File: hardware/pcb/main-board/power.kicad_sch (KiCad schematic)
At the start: 16 parts, among them SW501 NO POP, SW502 NO POP, U501 PT4110

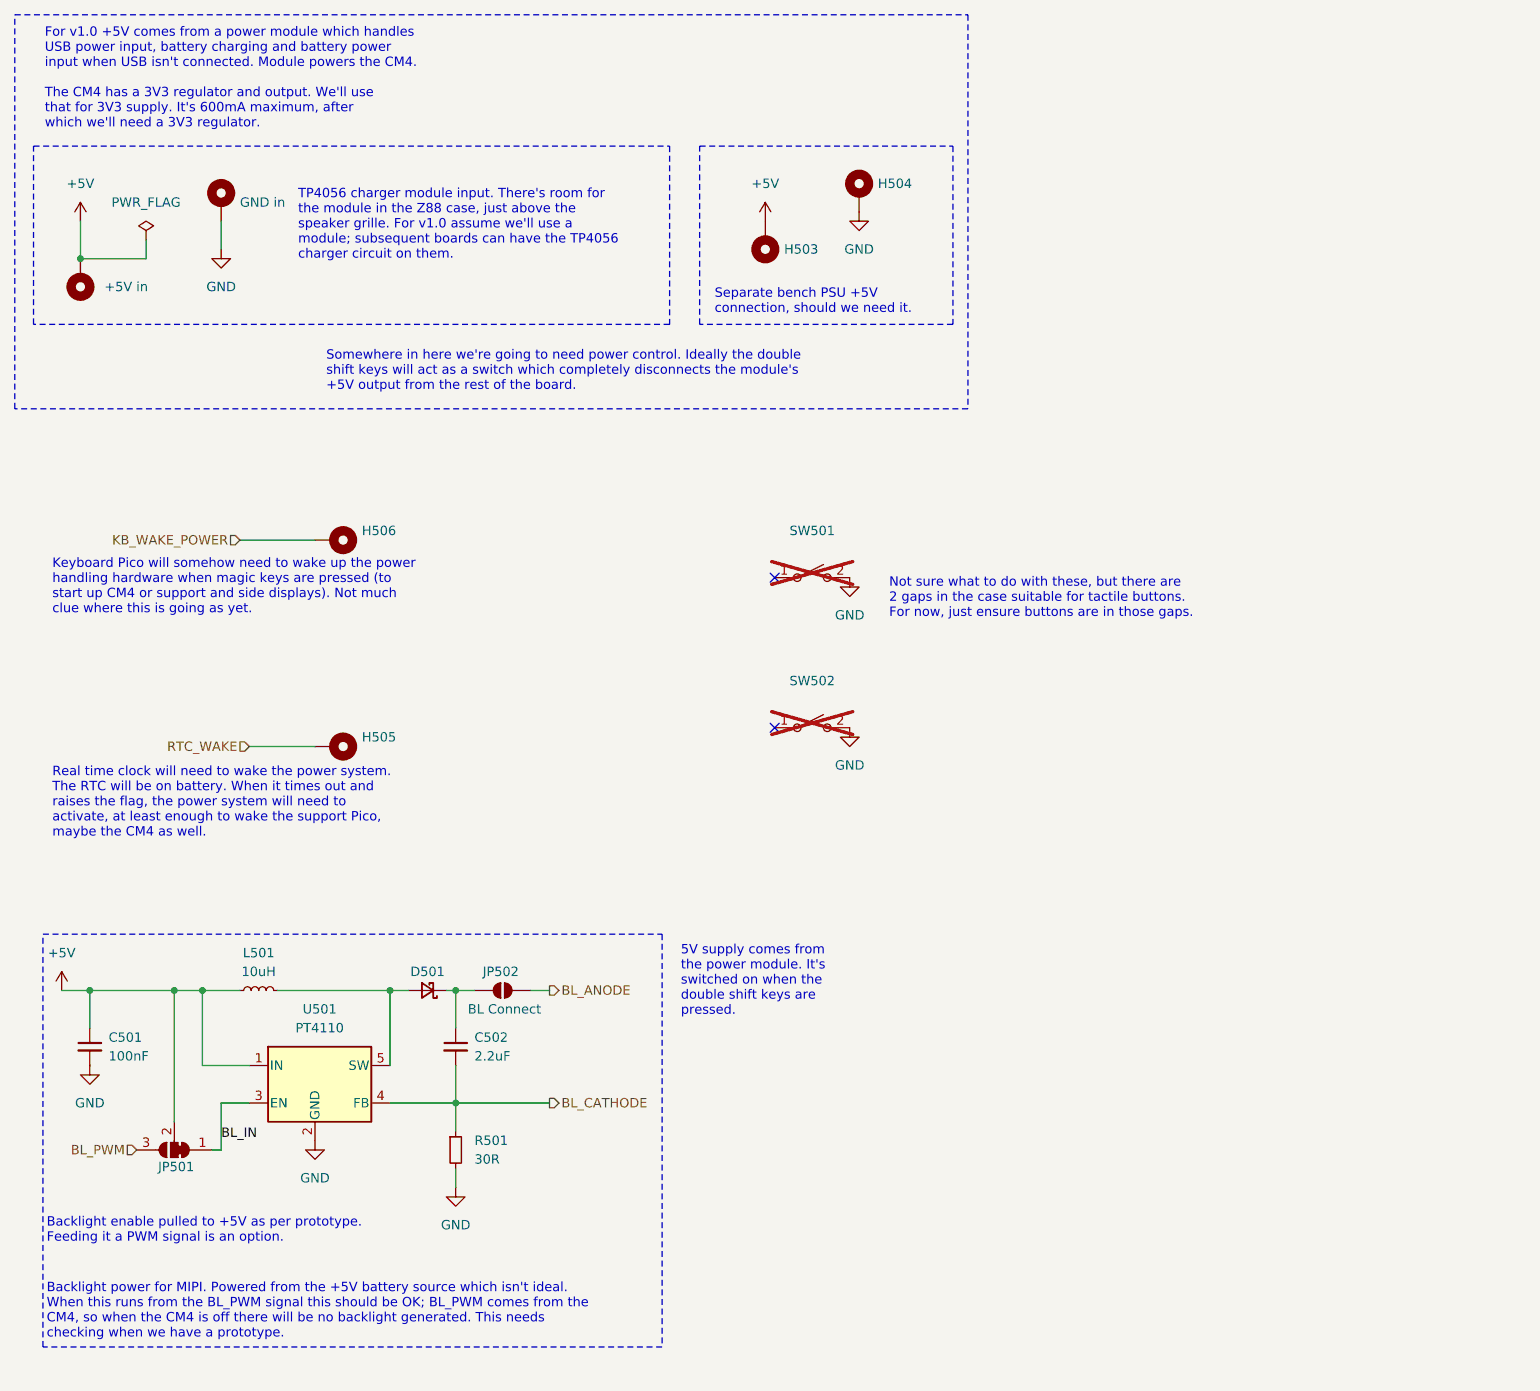
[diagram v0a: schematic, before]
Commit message: start next board iteration, add latch and pico power bits
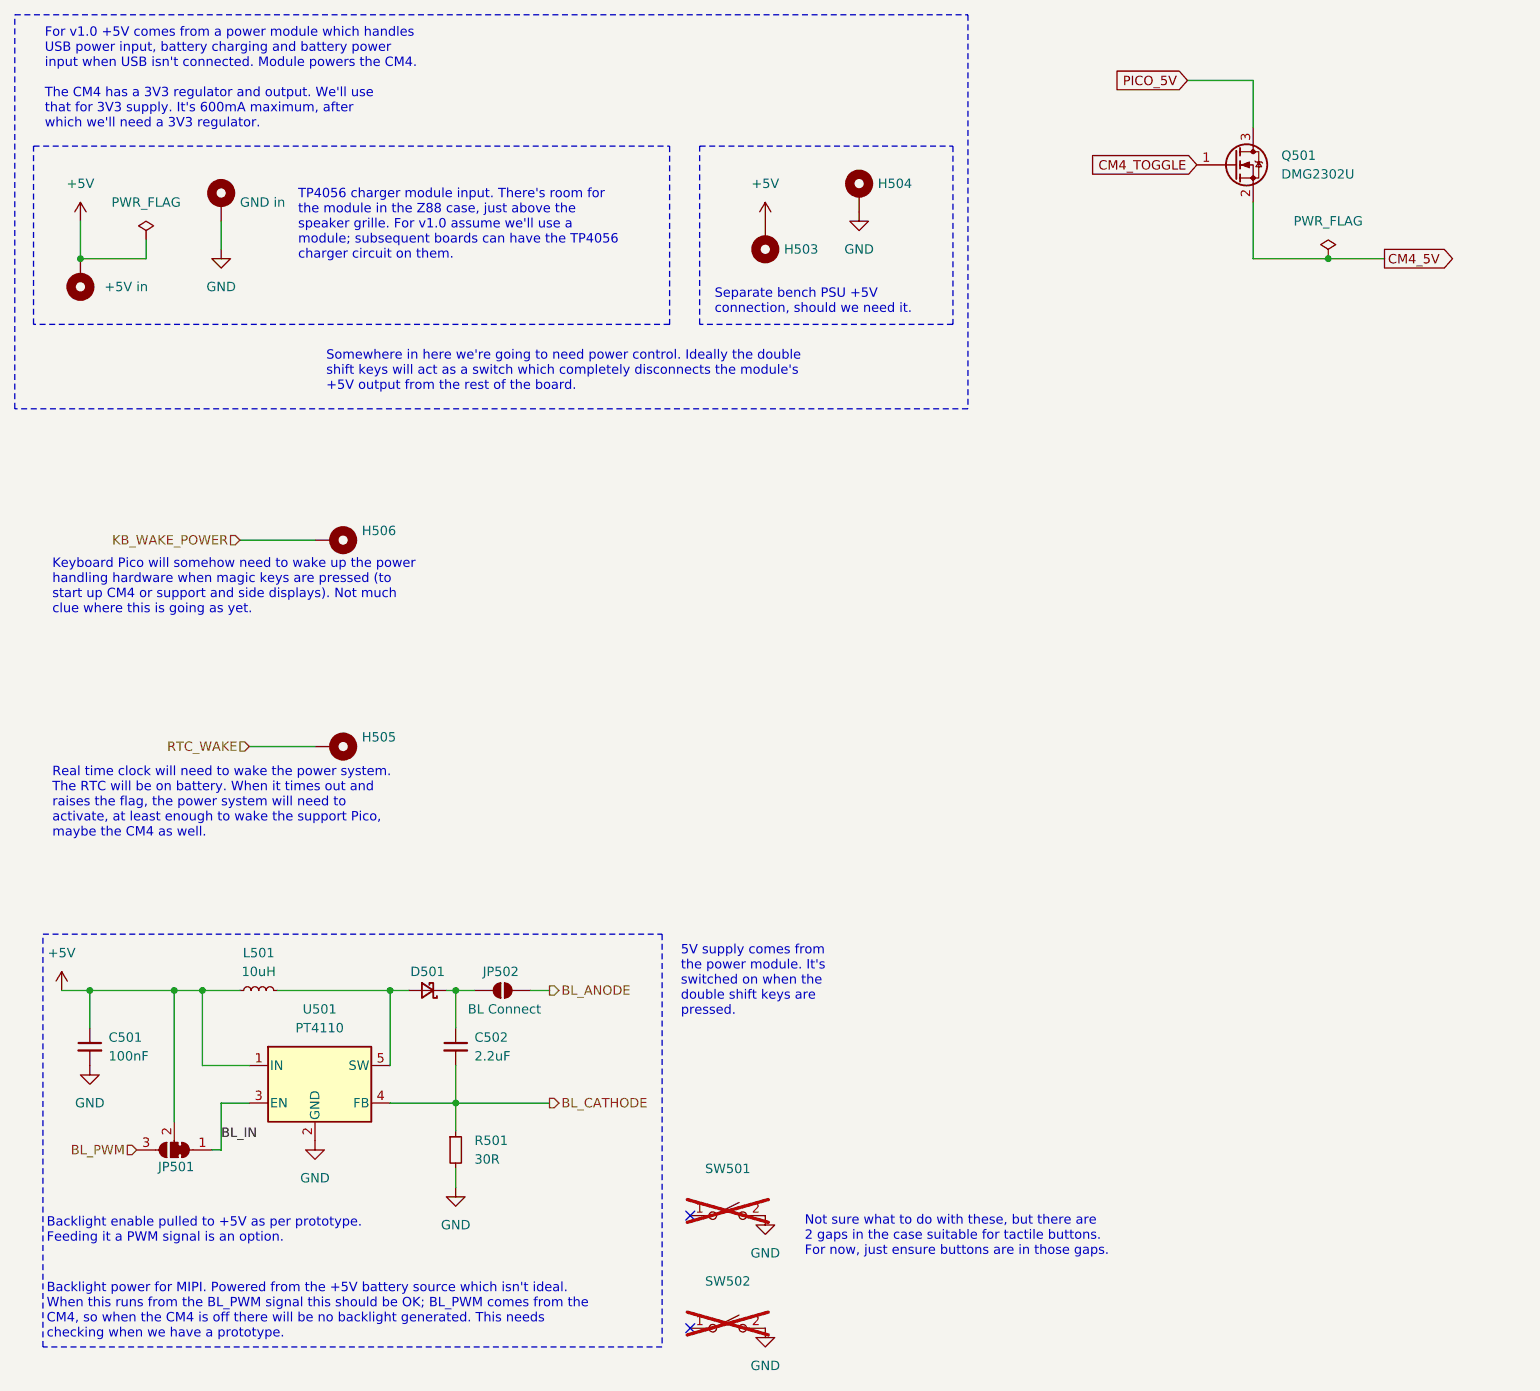
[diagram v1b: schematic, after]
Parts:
- added Q501: DMG2302U, Package_TO_SOT_SMD:SOT-23, symbol Transistor_FET:DMG2302U
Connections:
- new net CM4_5V: Q501.2 (S)
- new net CM4_TOGGLE: Q501.1 (G)
- new net PICO_5V: Q501.3 (D)
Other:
- moved on the sheet: SW501, SW502

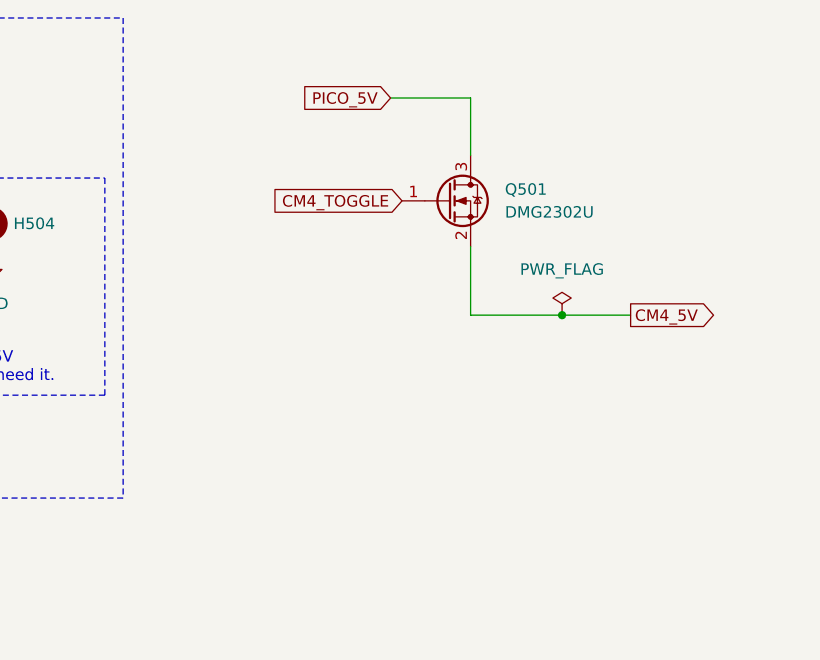
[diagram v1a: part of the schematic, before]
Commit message: CM4 power switch
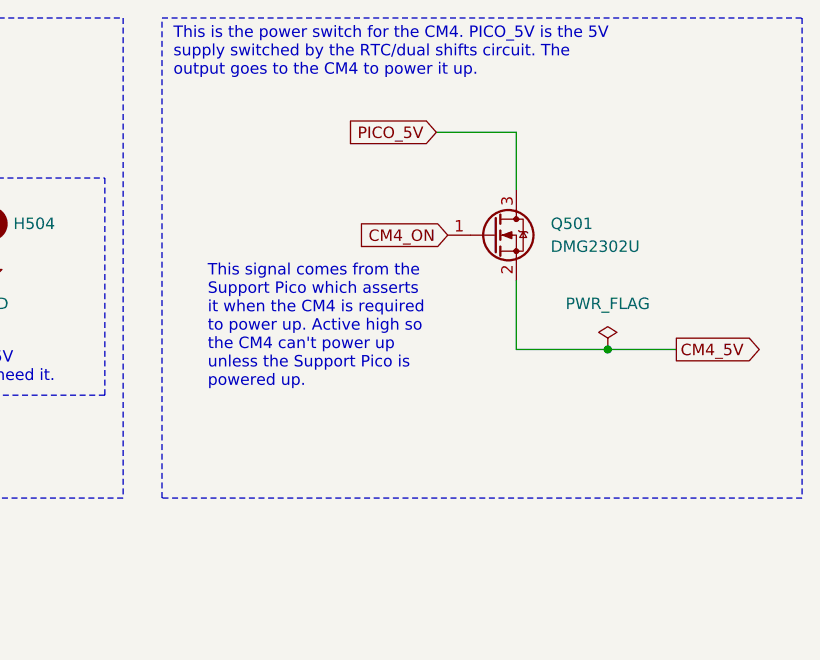
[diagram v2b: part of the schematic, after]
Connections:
- net CM4_TOGGLE renamed CM4_ON
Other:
- note added: "This is the power switch for the CM4. PICO_5V is the 5V supply switched by the RTC/dual shifts circuit. The output goes to the CM4 to power it up."
- note added: "This signal comes from the Support Pico which asserts it when the CM4 is required to power up. Active high so the CM4 can't power up unless the Support Pico is powered up."
- moved on the sheet: Q501
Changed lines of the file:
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@@
 	)
 	(junction
-		(at 190.5 46.99)
+		(at 195.58 50.8)
 		(diameter 0)
 		(color 0 0 0 0)
@@
 	(wire
 		(pts
-			(xy 180.34 22.86) (xy 180.34 29.21)
+			(xy 185.42 26.67) (xy 185.42 33.02)
 		)
 		(stroke
@@
 	(wire
 		(pts
-			(xy 180.34 39.37) (xy 180.34 46.99)
+			(xy 185.42 43.18) (xy 185.42 50.8)
 		)
 		(stroke
@@
 	(wire
 		(pts
-			(xy 171.45 22.86) (xy 180.34 22.86)
-		)
-		(stroke
-			(width 0)
-			(type default)
-		)
-	)
-	(wire
-		(pts
-			(xy 180.34 46.99) (xy 190.5 46.99)
+			(xy 176.53 26.67) (xy 185.42 26.67)
+		)
+		(stroke
+			(width 0)
+			(type default)
+		)
+	)
+	(wire
+		(pts
+			(xy 185.42 50.8) (xy 195.58 50.8)
 		)
 		(stroke
@@
 	(wire
 		(pts
-			(xy 190.5 46.99) (xy 198.12 46.99)
+			(xy 195.58 50.8) (xy 203.2 50.8)
 		)
 		(stroke
@@
 		(start 105.41 31.75)
 		(end 139.7 55.88)
+		(stroke
+			(width 0)
+			(type dash)
+		)
+		(fill
+			(type none)
+		)
+	)
+	(rectangle
+		(start 146.05 13.97)
+		(end 217.17 67.31)
 		(stroke
 			(width 0)
@@
 		)
 	)
+	(text "This signal comes from the\nSupport Pico which asserts\nit when the CM4 is required\nto power up. Active high so\nthe CM4 can't power up\nunless the Support Pico is\npowered up."
+		(exclude_from_sim no)
+		(at 151.13 48.26 0)
+		(effects
+			(font
+				(size 1.27 1.27)
+			)
+			(justify left)
+		)
+	)
 	(text "TP4056 charger module input. There's room for\nthe module in the Z88 case, just above the\nspeaker grille. For v1.0 assume we'll use a\nmodule; subsequent boards can have the TP4056\ncharger circuit on them."
 		(exclude_from_sim no)
@@
 		(exclude_from_sim no)
 		(at 17.78 91.44 0)
+		(effects
+			(font
+				(size 1.27 1.27)
+			)
+			(justify left)
+		)
+	)
+	(text "This is the power switch for the CM4. PICO_5V is the 5V\nsupply switched by the RTC/dual shifts circuit. The\noutput goes to the CM4 to power it up."
+		(exclude_from_sim no)
+		(at 147.32 17.78 0)
 		(effects
 			(font
@@
 		)
 	)
-	(global_label "CM4_TOGGLE"
+	(global_label "CM4_ON"
 		(shape input)
-		(at 172.72 34.29 180)
+		(at 177.8 38.1 180)
 		(fields_autoplaced yes)
 		(effects
@@
 		)
 		(property "Intersheetrefs" "${INTERSHEET_REFS}"
-			(at 158.4753 34.29 0)
+			(at 167.9095 38.1 0)
 			(effects
 				(font
@@
 	(global_label "PICO_5V"
 		(shape input)
-		(at 171.45 22.86 180)
+		(at 176.53 26.67 180)
 		(fields_autoplaced yes)
 		(effects
@@
 		)
 		(property "Intersheetrefs" "${INTERSHEET_REFS}"
-			(at 161.378 22.86 0)
+			(at 166.458 26.67 0)
 			(effects
 				(font
@@
 	(global_label "CM4_5V"
 		(shape output)
-		(at 198.12 46.99 0)
+		(at 203.2 50.8 0)
 		(fields_autoplaced yes)
 		(effects
@@
 		)
 		(property "Intersheetrefs" "${INTERSHEET_REFS}"
-			(at 207.6476 46.99 0)
+			(at 212.7276 50.8 0)
 			(effects
 				(font
@@
 	(symbol
 		(lib_id "Transistor_FET:DMG2302U")
-		(at 177.8 34.29 0)
+		(at 182.88 38.1 0)
 		(unit 1)
 		(exclude_from_sim no)
@@
 		(fields_autoplaced yes)
 		(property "Reference" "Q501"
-			(at 184.15 33.0199 0)
+			(at 189.23 36.8299 0)
 			(effects
 				(font
@@
 		)
 		(property "Value" "DMG2302U"
-			(at 184.15 35.5599 0)
+			(at 189.23 39.3699 0)
 			(effects
 				(font
@@
 		)
 		(property "Footprint" "Package_TO_SOT_SMD:SOT-23"
-			(at 182.88 36.195 0)
+			(at 187.96 40.005 0)
 			(effects
 				(font
@@
 		)
 		(property "Datasheet" "http://www.diodes.com/assets/Datasheets/DMG2302U.pdf"
+			(at 187.96 41.91 0)
+			(effects
+				(font
+					(size 1.27 1.27)
+				)
+				(justify left)
+				(hide yes)
+			)
+		)
+		(property "Description" "4.2A Id, 20V Vds, N-Channel MOSFET, SOT-23"
 			(at 182.88 38.1 0)
-			(effects
-				(font
-					(size 1.27 1.27)
-				)
-				(justify left)
-				(hide yes)
-			)
-		)
-		(property "Description" "4.2A Id, 20V Vds, N-Channel MOSFET, SOT-23"
-			(at 177.8 34.29 0)
 			(effects
 				(font
@@
 	(symbol
 		(lib_id "power:PWR_FLAG")
-		(at 190.5 46.99 0)
+		(at 195.58 50.8 0)
 		(unit 1)
 		(exclude_from_sim no)
@@
 		(fields_autoplaced yes)
 		(property "Reference" "#FLG502"
-			(at 190.5 45.085 0)
+			(at 195.58 48.895 0)
 			(effects
 				(font
@@
 		)
 		(property "Value" "PWR_FLAG"
-			(at 190.5 41.91 0)
+			(at 195.58 45.72 0)
 			(effects
 				(font
@@
 		)
 		(property "Footprint" ""
-			(at 190.5 46.99 0)
+			(at 195.58 50.8 0)
 			(effects
 				(font
@@
 		)
 		(property "Datasheet" "~"
-			(at 190.5 46.99 0)
+			(at 195.58 50.8 0)
 			(effects
 				(font
@@
 		)
 		(property "Description" "Special symbol for telling ERC where power comes from"
-			(at 190.5 46.99 0)
-			(effects
-				(font
+			(at 195.58 50.8 0)
+			(effects
+				(font

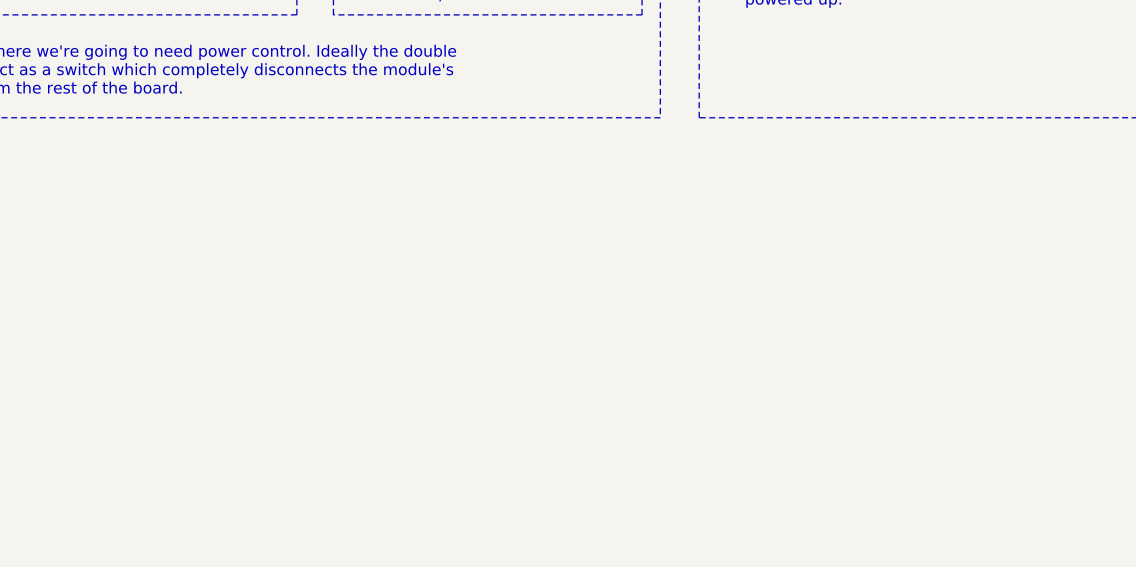
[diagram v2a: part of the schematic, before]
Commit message: make a start on RP2040 to replace the KB pico
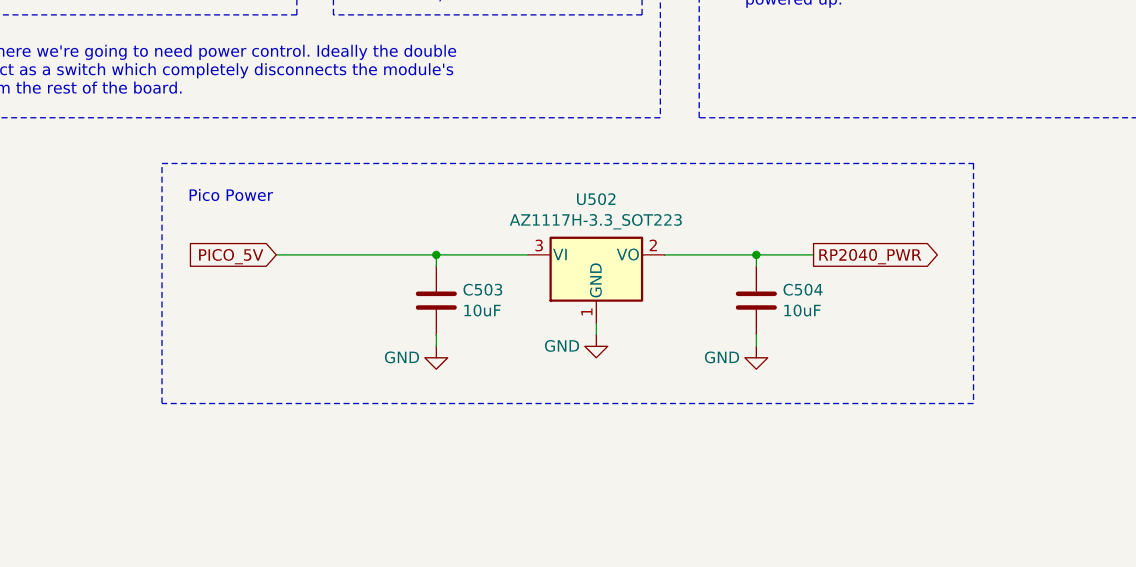
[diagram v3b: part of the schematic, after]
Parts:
- added C503, C504: 10uF, Capacitor_SMD:C_0805_2012Metric, symbol Device:C
- added U502: AZ1117H-3.3_SOT223, Package_TO_SOT_SMD:SOT-223-3_TabPin2, symbol Regulator_Linear:NCP1117-3.3_SOT223
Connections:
- net GND: now also C503.2, C504.2, U502.1 (GND)
- net PICO_5V: now also C503.1, U502.3 (VI)
- new net RP2040_PWR: C504.1, U502.2 (VO)
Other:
- note added: "Pico Power"
- title: Z88R - Z88 Recreated -> Z88R - Z88 Recreation

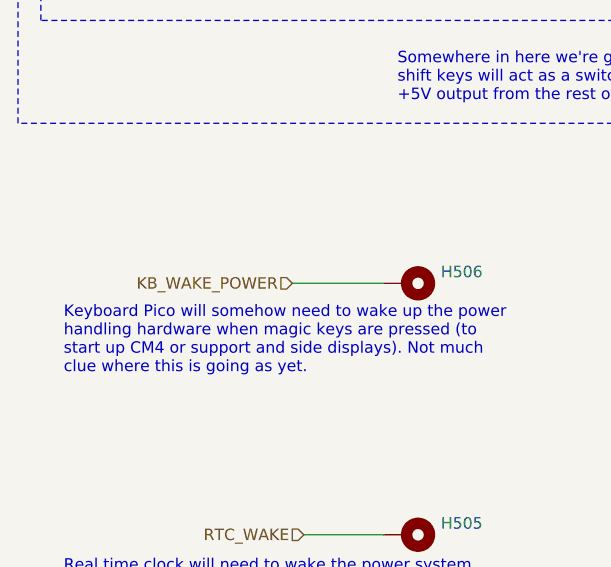
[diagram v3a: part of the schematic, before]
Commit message: more working out of the KB pico replacement
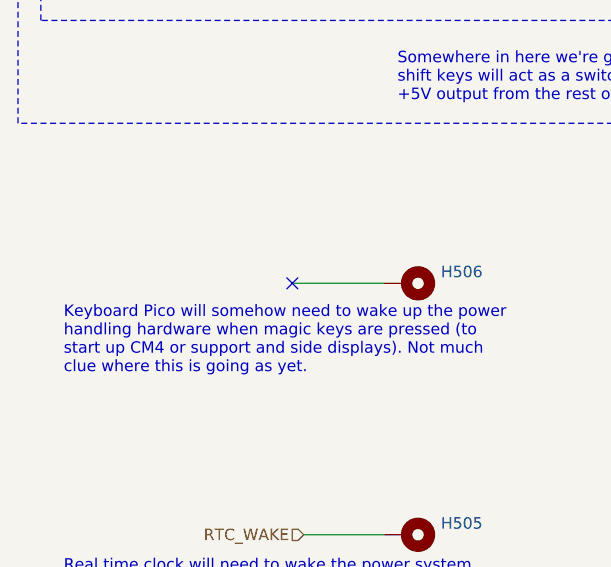
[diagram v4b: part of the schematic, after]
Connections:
- net KB_WAKE_POWER: no longer names the net of H506.1
- no-connect marks 2 -> 3
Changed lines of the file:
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@@
+	)
+	(no_connect
+		(at 43.18 85.09)
 	)
 	(no_connect
@@
 		)
 	)
-	(hierarchical_label "KB_WAKE_POWER"
-		(shape input)
-		(at 43.18 85.09 180)
-		(effects
-			(font
-				(size 1.27 1.27)
-			)
-			(justify right)
-		)
-	)
